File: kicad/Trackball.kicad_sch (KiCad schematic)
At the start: 49 parts, among them J1 Conn_01x04, J10 Conn_01x01_Female, J3 Conn_02x03_Odd_Even, J4 Conn_01x06_Pin, J7 Conn_01x01_Female, SW1 Push_Button, SW101 Push_Button, SW104 Push_Button, SW2 Push_Button, SW3 RotaryEncoder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

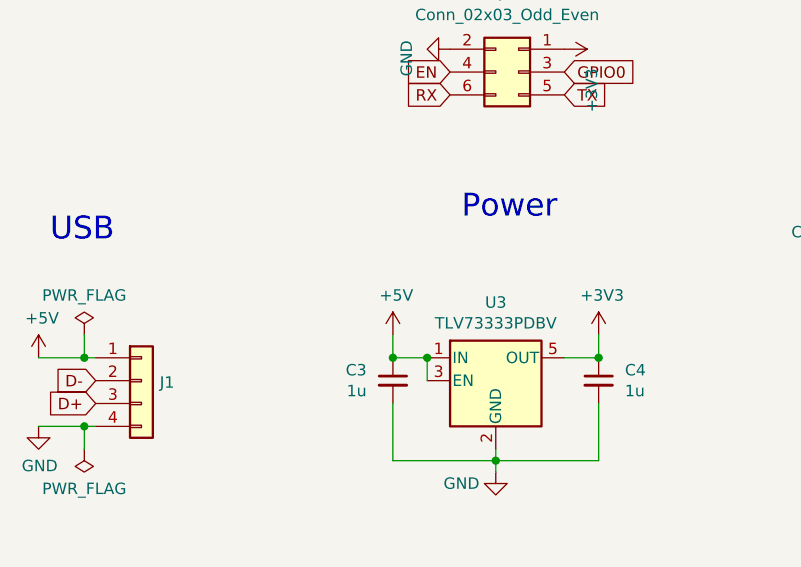
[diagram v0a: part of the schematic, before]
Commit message: changement de taille
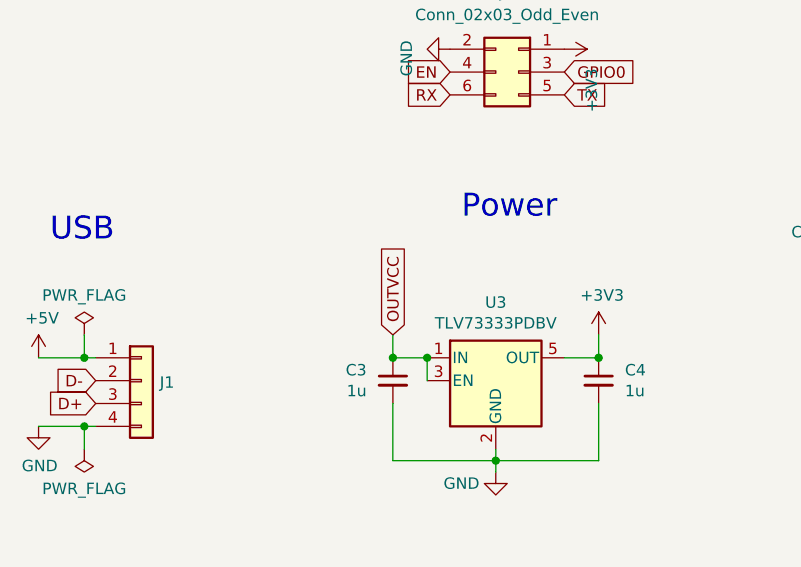
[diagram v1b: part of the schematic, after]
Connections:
- net +5V: no longer C3.1, U3.1 (IN), U3.3 (EN)
- net BAT+: now also C3.1, U3.1 (IN), U3.3 (EN)
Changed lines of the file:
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@@
 	(label "G1"
 		(at 149.86 -167.64 0)
+		(fields_autoplaced yes)
 		(effects
 			(font
@@
 	(label "OC"
 		(at 143.51 -158.75 0)
+		(fields_autoplaced yes)
 		(effects
 			(font
@@
 	(label "S1"
 		(at 158.75 -168.91 0)
+		(fields_autoplaced yes)
 		(effects
 			(font
@@
 	(label "OUTGND"
 		(at 171.45 -134.62 0)
+		(fields_autoplaced yes)
 		(effects
 			(font
@@
 	(label "G2"
 		(at 144.78 -143.51 0)
+		(fields_autoplaced yes)
 		(effects
 			(font
@@
 		)
 	)
+	(global_label "OUTVCC"
+		(shape input)
+		(at 67.31 -57.15 90)
+		(fields_autoplaced yes)
+		(effects
+			(font
+				(size 1.27 1.27)
+			)
+			(justify left)
+		)
+		(property "Intersheetrefs" "${INTERSHEET_REFS}"
+			(at 67.31 -66.7382 90)
+			(effects
+				(font
+					(size 1.27 1.27)
+				)
+				(justify left)
+				(hide yes)
+			)
+		)
+	)
 	(global_label "BAT-"
 		(shape input)
@@
 			)
 		)
-		(property "Datasheet" ""
+		(property "Datasheet" "https://www.lcsc.com/datasheet/lcsc_datasheet_2010271837_FUXINSEMI-FS8205A_C908265.pdf"
 			(at 149.86 -149.86 0)
 			(effects
@@
 					(unit 1)
 				)
-			)
-		)
-	)
-	(symbol
-		(lib_id "Trackball-rescue:+5V-power")
-		(at 67.31 -57.15 0)
-		(unit 1)
-		(exclude_from_sim no)
-		(in_bom yes)
-		(on_board yes)
-		(dnp no)
-		(property "Reference" "#PWR011"
-			(at 67.31 -53.34 0)
-			(effects
-				(font
-					(size 1.27 1.27)
-				)
-				(hide yes)
-			)
-		)
-		(property "Value" "+5V"
-			(at 67.691 -61.5442 0)
-			(effects
-				(font
-					(size 1.27 1.27)
-				)
-			)
-		)
-		(property "Footprint" ""
-			(at 67.31 -57.15 0)
-			(effects
-				(font
-					(size 1.27 1.27)
-				)
-				(hide yes)
-			)
-		)
-		(property "Datasheet" ""
-			(at 67.31 -57.15 0)
-			(effects
-				(font
-					(size 1.27 1.27)
-				)
-				(hide yes)
-			)
-		)
-		(property "Description" ""
-			(at 67.31 -57.15 0)
-			(effects
-				(font
-					(size 1.27 1.27)
-				)
-				(hide yes)
-			)
-		)
-		(pin "1"
-		)
-		(instances
-			(project "Trackball"
-				(path "/0da53b0a-8f1e-4a10-82c1-3eecfed721ae"
-					(reference "#PWR011")
-					(unit 1)
-				)

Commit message: repos
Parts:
- removed SW101: Push_Button, PCM_openinput:SW_Micro_Switch, symbol PCM_SL_Devices:Push_Button
- removed SW104: Push_Button, MaSe:SW_Micro_Switch, symbol PCM_SL_Devices:Push_Button

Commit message: next routing try
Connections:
- net CenterClick: now also U4.7 (GPIO7/TOUCH7/ADC1_CH6); no longer U4.17 (GPIO9/TOUCH9/ADC1_CH8/FSPIHD/SUBSPIHD)
- net LED1: now also U4.9 (GPIO16/U0CTS/ADC2_CH5/XTAL_32K_N); no longer U4.16 (GPIO46)
- net LED2: now also U4.8 (GPIO15/U0RTS/ADC2_CH4/XTAL_32K_P); no longer U4.28 (SPIIO6/GPIO35/FSPID/SUBSPID)
- net PROG_TP40: now reaches R5.1, U5.2 (PROG)
- net VCC_DW01: now reaches C9.1, R8.2, U6.5 (VCC)
- net CS_DW01: now reaches R6.2, U6.2 (CS)

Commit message: clean up for print test
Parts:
- removed H1: MountingHole, MountingHole:MountingHole_3.2mm_M3, symbol Mechanical:MountingHole
- added Brd1: SSD1306, Connector_PinHeader_2.54mm:PinHeader_1x04_P2.54mm_Vertical, symbol SSD1306-128x64_OLED:SSD1306
- added C10, C11: 0.1u, Capacitor_SMD:C_0805_2012Metric, symbol Device:C
- added Q2, Q3: BSS83P, Package_TO_SOT_SMD:SOT-23, symbol Transistor_FET:BSS83P
- added SW5, SW6: Push_Button, MaSe:SW_Micro_Switch, symbol PCM_SL_Devices:Push_Button
- added U8: NRF24L01_Breakout, RF_Module:nRF24L01_Breakout, symbol RF:NRF24L01_Breakout
- C7, C9: value 0.1uF -> 0.1u; footprint Capacitor_SMD:C_0805_2012Metric_Pad1.18x1.45mm_HandSolder -> Capacitor_SMD:C_0805_2012Metric; LCSC (none) -> C14663
- R5: footprint Resistor_SMD:R_0805_2012Metric_Pad1.20x1.40mm_HandSolder -> Resistor_SMD:R_0805_2012Metric
- R6: footprint Resistor_SMD:R_0603_1608Metric_Pad0.98x0.95mm_HandSolder -> Resistor_SMD:R_0805_2012Metric
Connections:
- net +3V3: now also Q2.2 (S), Q3.2 (S)
- net CenterClick: now also U4.10 (GPIO17/U1TXD/ADC2_CH6); no longer U4.7 (GPIO7/TOUCH7/ADC1_CH6)
- net Earth: now also Brd1.1 (GND), C10.2, C11.2, SW5.1, SW6.1, U8.1 (GND)
- net MISO: now also U8.7 (MISO)
- net MOSI: now also U8.6 (MOSI)
- net SCLK: now also U8.5 (SCK)
- net leftClick: now also SW5.2
- net rightClick: now also SW6.2
- net CE_24: now reaches U4.16 (GPIO46)
- net CE_24: now also U8.3 (CE)
- net CSN_24: now reaches U4.17 (GPIO9/TOUCH9/ADC1_CH8/FSPIHD/SUBSPIHD)
- net CSN_24: now also U8.4 (~{CSN})
- net NRF_COM_PO: now reaches U4.38 (GPIO2/TOUCH2/ADC1_CH1)
- net NRF_COM_PO: now also Q3.1 (G)
- net SCL_DISPLAY: now reaches U4.4 (GPIO4/TOUCH4/ADC1_CH3)
- net SCL_DISPLAY: now also Brd1.3 (SCL)
- net SDA_DISPLAY: now reaches U4.5 (GPIO5/TOUCH5/ADC1_CH4)
- net SDA_DISPLAY: now also Brd1.4 (SDA)
- net DSP_COM_PO: now reaches U4.6 (GPIO6/TOUCH6/ADC1_CH5)
- net DSP_COM_PO: now also Q2.1 (G)
- new net IRQ_24: U4.7 (GPIO7/TOUCH7/ADC1_CH6), U8.8 (IRQ)
- new net VCC_DISP: Brd1.2 (VCC), C10.1, Q2.3 (D)
- new net VCC_NRF: C11.1, Q3.3 (D), U8.2 (VCC)

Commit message: e
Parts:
- removed Brd1: SSD1306, Connector_PinHeader_2.54mm:PinHeader_1x04_P2.54mm_Vertical, symbol SSD1306-128x64_OLED:SSD1306
- removed C10: 0.1u, Capacitor_SMD:C_0805_2012Metric, symbol Device:C
- removed D101, D102: LED_3mm, LED_THT:LED_D3.0mm, symbol PCM_SL_Devices:LED_3mm
- removed Q2, Q3: BSS83P, Package_TO_SOT_SMD:SOT-23, symbol Transistor_FET:BSS83P
- removed R105, R106: R_1206, PCM_4ms_Resistor:R_0805_2012Metric, symbol PCM_Resistor_AKL:R_1206
- removed SW1, SW2: Push_Button, MaSe:SW_Hotswap_Kailh_Choc_V1V2_1.00u, symbol PCM_SL_Devices:Push_Button
- removed SW5: Push_Button, MaSe:SW_Micro_Switch, symbol PCM_SL_Devices:Push_Button
- added H1, H5, H6, H7, H8: MountingHole, MountingHole:MountingHole_2.5mm, symbol Mechanical:MountingHole
- added SW1: SW_SPDT_XKB_DMx-xxxx-1, MaSe:SW_Micro_Switch, symbol Switch:SW_SPDT_XKB_DMx-xxxx-1
- H2, H3, H4: footprint MountingHole:MountingHole_3.2mm_M3 -> MountingHole:MountingHole_2.5mm
- U8: footprint RF_Module:nRF24L01_Breakout -> sensors_radios:NRF24L01-SMD
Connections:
- net VCC_NRF is gone; now on net +3V3: C11.1, U8.2 (VCC)
- net Earth: now also SW1.2 (B), SW1.3 (C)
- net leftClick: now also SW1.1 (A)
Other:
- moved on the sheet: J7
